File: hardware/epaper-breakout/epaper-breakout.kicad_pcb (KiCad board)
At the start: 2 copper layers, 99.6 x 31.2 mm, 68 parts, among them J1 XF2M-3315-1A, J2 C10418, J3 Conn_02x06_Counter_Clockwise, J4 ED060SC4, Q1 IRLML6402, U1 MCP1700-3302E_SOT23, U2 LT1945, U3 LT1945, U5 ESP32-WROVER, U6 CH330N, U7 LM358, U8 74HC4094-normal, U9 MCP9700AT-ETT

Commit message: WIP: partial routing
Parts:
- removed BOOT1: SW2, epaper-breakout:SW_TS-1187A
- removed RESET1: SW1, epaper-breakout:SW_TS-1187A
- added Q2: AO3401A, Package_TO_SOT_SMD:SOT-23, F.Cu at (70.9, 77.8)
- added Q3: MMBT3904, Package_TO_SOT_SMD:SOT-23, F.Cu at (38.4, 64.8)
- added Q4: MMBT3904, Package_TO_SOT_SMD:SOT-23, F.Cu at (34.0, 69.4)
- added Q5: AO3401A, Package_TO_SOT_SMD:SOT-23, F.Cu at (75.4, 77.8)
- added Q6: MMBT3904, Package_TO_SOT_SMD:SOT-23, F.Cu at (68.3, 70.3)
- added R1: 10k, Resistor_SMD:R_0805_2012Metric, F.Cu at (38.4, 68.6)
- added R20: 10k, Resistor_SMD:R_0805_2012Metric, F.Cu at (70.9, 81.5)
- added R21: 10k, Resistor_SMD:R_0805_2012Metric, F.Cu at (75.3, 81.5)
- added U10: ED060SC7, epaper-breakout:AXT334124, F.Cu at (118.6, 57.5)
- added U4: CH340G, Package_SO:SOIC-16_3.9x9.9mm_P1.27mm, F.Cu at (27.5, 68.3)
- added Y1: Crystal_GND2, Crystal:Crystal_SMD_3225-4Pin_3.2x2.5mm_HandSoldering, F.Cu at (60.9, 70.2)
- C13, C14: value 0.1uF -> 10pF
- C15, C16: value 1nF -> 0.1uF
- J4: moved to F.Cu
- Q1: value IRLML6402 -> MMBT3904
- R11: value 470 -> 10k
- R12: value 470 -> 1k
- U6: value CH330N -> ED060XC5; footprint Package_SO:SOIC-8_3.9x4.9mm_P1.27mm -> epaper-breakout:X05A20H34G
- moved R11 61.0 mm to (42.8, 68.6), turned to 0 degrees
- moved U6 49.3 mm to (70.6, 54.7), turned to 0 degrees
- moved Q1 44.3 mm to (66.5, 77.8), turned to 0 degrees
- moved U9 36.1 mm to (83.7, 21.7)
- moved R12 33.2 mm to (66.5, 81.5), turned to 0 degrees
- moved U8 30.9 mm to (77.2, 25.1)
- moved C16 27.1 mm to (42.6, 71.3), turned to 0 degrees
- moved J4 23.9 mm to (104.3, 56.1), turned to 0 degrees
- moved U5 22.8 mm to (95.9, 26.2), turned to 0 degrees
- moved C15 18.6 mm to (82.3, 67.9)
- moved R10 16.9 mm to (79.1, 66.3)
- moved R13 16.5 mm to (94.7, 8.20)
- moved R15 15.1 mm to (90.1, 9.80)
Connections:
- C1 pad 1: EPD_POWER -> SW_VIN
- C13 pad 1: /+3.3V -> Net-(C13-Pad1)
- C14 pad 1: /+3.3V -> GND
- C14 pad 2: GND -> Net-(C14-Pad2)
- C15 pad 1: GND -> /EN
- C15 pad 2: /EN -> GND
- C16 pad 1: GND -> /+3.3V
- C16 pad 2: Net-(C16-Pad2) -> GND
- C6 pad 1: EPD_POWER -> SW_VIN
- J1 pad 11: /+3.3V -> EPD_VDD
- J1 pad 30: /+3.3V -> EPD_VDD
- J1 pad 7: /+3.3V -> EPD_VDD
- J4 pad 10: /+3.3V -> EPD_VDD
- J4 pad 29: /+3.3V -> EPD_VDD
- J4 pad 30: /+3.3V -> EPD_VDD
- J4 pad 35: /+3.3V -> EPD_VDD
- J4 pad 36: /+3.3V -> EPD_VDD
- J4 pad 4: /+3.3V -> EPD_VDD
- J4 pad 8: /+3.3V -> EPD_VDD
- L1 pad 2: EPD_POWER -> SW_VIN
- L2 pad 2: EPD_POWER -> SW_VIN
- L3 pad 2: EPD_POWER -> SW_VIN
- L4 pad 2: EPD_POWER -> SW_VIN
- Q1 pad 1: /~SMPS_CTRL -> Net-(Q1-Pad1)
- Q1 pad 2: 5V -> GND
- Q1 pad 3: EPD_POWER -> Net-(Q1-Pad3)
- R11 pad 1: /EP_D3 -> Net-(Q4-Pad1)
- R11 pad 2: Net-(BOOT1-Pad2) -> /~RTS
- R12 pad 1: /EN -> Net-(Q1-Pad1)
- R12 pad 2: Net-(C16-Pad2) -> /SMPS_CTRL
- U2 pad 8: EPD_POWER -> SW_VIN
- U3 pad 8: EPD_POWER -> SW_VIN
- U6 pad 1: Net-(J2-Pad3) -> /-15V
- U6 pad 2: Net-(J2-Pad2) -> /-20V
- U6 pad 5: /+3.3V -> (no net)
- U6 pad 6: /USB_TXD -> EPD_VDD
- U6 pad 7: /USB_RXD -> GND
- U6 pad 8: /+3.3V -> /EP_CKH
- U8 pad 4: /~SMPS_CTRL -> /SMPS_CTRL
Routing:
- net /+3.3V: track 306.9 -> 8.42 mm, vias 13 -> 1
- net GND: track 368.8 -> 187.1 mm, vias 122 -> 62
- net /EP_STV: track 37.3 -> 139.0 mm, vias 1 -> 5
- net /+22V: track 115.5 -> 210.9 mm, vias 2 -> 7
- net EPD_VDD: track 0.00 -> 94.2 mm, vias 0 -> 6
- net /EP_MODE: track 46.7 -> 138.2 mm, vias 1 -> 5
- net SW_VIN: track 0.00 -> 81.7 mm, vias 0 -> 4
- net EPD_POWER: track 81.7 -> 0.00 mm, vias 4 -> 0
- net /A1: track 126.2 -> 46.3 mm, vias 1 -> 0
- net /EP_D6: track 41.9 -> 118.7 mm, vias 3 -> 6
- net /EP_D5: track 43.6 -> 117.2 mm, vias 3 -> 6
- net /EP_D7: track 48.5 -> 119.5 mm, vias 3 -> 5
- net /EP_D2: track 39.2 -> 109.3 mm, vias 1 -> 6
- net /EP_VCOM: track 95.0 -> 159.7 mm, vias 2 -> 6
- net /EP_OE: track 50.9 -> 114.4 mm, vias 3 -> 7
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- removed copper zone on B.Cu, net GND
- removed copper zone on F.Cu, net GND
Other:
- board size 99.6 x 31.2 mm -> 100 x 40.5 mm
- net class Default: clearance 0.2 -> 0.16
- rule trace_clearance: 0.2 -> 0.16

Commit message: partial routing
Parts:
- removed Q1: MMBT3904, Package_TO_SOT_SMD:SOT-23
- removed R2, R21, R3, R8, R9: 10k, Resistor_SMD:R_0805_2012Metric
- moved R12 53.3 mm to (70.6, 28.4), turned to 90 degrees
- moved R20 51.7 mm to (44.8, 36.8), turned to 180 degrees
- moved Q2 51.6 mm to (43.9, 33.8), turned to 270 degrees
- moved R13 49.7 mm to (108.0, 56.1), turned to 270 degrees
- moved R15 46.2 mm to (108.0, 52.4), turned to 90 degrees
- moved C16 42.8 mm to (32.3, 29.7)
- moved Q6 38.1 mm to (69.8, 32.3), turned to 270 degrees
- moved Y1 36.9 mm to (34.5, 44.3), turned to 180 degrees
- moved Q5 35.3 mm to (78.7, 42.7)
- moved R11 33.8 mm to (35.8, 35.5), turned to 180 degrees
- moved Q4 33.5 mm to (39.3, 36.3)
- moved U4 32.2 mm to (29.4, 36.1)
- moved C15 30.6 mm to (78.7, 37.6), turned to 0 degrees
- moved R1 29.3 mm to (35.8, 39.3), turned to 180 degrees
- moved R10 26.7 mm to (78.7, 39.6), turned to 180 degrees
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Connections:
- Q4 pad 3: /EP_D3 -> /EP_D0
- Q5 pad 1: Net-(Q1-Pad3) -> Net-(Q2-Pad1)
- R13 pad 1: /EP_D4 -> /EP_LE
- R15 pad 1: /EP_D3 -> /+3.3V
- R15 pad 2: /+3.3V -> /EP_D0
- U5 pad 10: /EP_CKV -> Net-(U5-Pad10)
- U5 pad 11: /EP_STH -> /EP_CKV
- U5 pad 12: /EP_D5 -> /EP_STH
- U5 pad 23: /EP_LE -> /EP_CKH
- U5 pad 24: /EP_D4 -> /EP_LE
- U5 pad 25: /EP_D3 -> /EP_D0
- U5 pad 26: /EP_D2 -> /EP_D1
- U5 pad 29: /EP_CKH -> /EP_D2
- U5 pad 30: Net-(U5-Pad30) -> /EP_D3
- U5 pad 31: Net-(U5-Pad31) -> /EP_D4
- U5 pad 33: /EP_D6 -> /EP_D5
- U5 pad 36: /EP_D7 -> /EP_D6
- U5 pad 37: Net-(U5-Pad37) -> /EP_D7
- U5 pad 8: /EP_D1 -> Net-(U5-Pad8)
- U5 pad 9: /EP_D0 -> Net-(U5-Pad9)
- U8 pad 1: Net-(U5-Pad31) -> Net-(U5-Pad10)
- U8 pad 2: Net-(U5-Pad37) -> Net-(U5-Pad9)
- U8 pad 3: Net-(U5-Pad30) -> Net-(U5-Pad8)
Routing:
- net GND: track 187.1 -> 12.6 mm, vias 62 -> 2
- net EPD_VDD: track 94.2 -> 188.3 mm, vias 6 -> 11
- net 5V: track 81.2 -> 0.00 mm, vias 2 -> 0
- net /15V: track 198.9 -> 127.1 mm
- net /MISO: track 57.6 -> 0.00 mm
- net /EP_D4: track 54.1 -> 110.9 mm, vias 5 -> 6
- net Net-(Q2-Pad1): track 0.00 -> 56.3 mm, vias 0 -> 2
- net /+22V: track 210.9 -> 157.3 mm, vias 7 -> 6
- net /MOSI: track 52.5 -> 0.00 mm, vias 1 -> 0
- net /SCLK: track 52.1 -> 0.00 mm
- net /SENSOR_VN: track 52.1 -> 0.00 mm
- net /SENSOR_VP: track 47.8 -> 0.00 mm
- net /A0: track 47.0 -> 0.00 mm
- net /A1: track 46.3 -> 0.00 mm
- net /EP_D3: track 60.3 -> 106.0 mm, vias 6 -> 4
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
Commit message: more routing
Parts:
- added C21: 10uF, Capacitor_SMD:C_0603_1608Metric, F.Cu at (48.3, 45.6)
- added C22: 0.1uF, Capacitor_SMD:C_0603_1608Metric, F.Cu at (48.3, 47.4)
- added C23: 0.1uF, Capacitor_SMD:C_0603_1608Metric, F.Cu at (45.5, 57.8)
- added D7: 1N5817, Diode_SMD:D_SOD-123, F.Cu at (43.1, 38.9)
- added D8: LED GREEN, LED_SMD:LED_0805_2012Metric, F.Cu at (43.6, 54.7)
- added D9: LED RED, LED_SMD:LED_0805_2012Metric, F.Cu at (43.6, 52.6)
- added J5: Conn_01x02_Male, Connector_PinHeader_2.54mm:PinHeader_1x02_P2.54mm_Vertical, F.Cu at (51.4, 57.7)
- added Q1: AO3401A, Package_TO_SOT_SMD:SOT-23, F.Cu at (48.1, 41.6)
- added R2: 100k, Resistor_SMD:R_0805_2012Metric, F.Cu at (51.1, 38.6)
- added R21: 100, Resistor_SMD:R_0805_2012Metric, F.Cu at (55.6, 57.7)
- added R22: 1k, Resistor_SMD:R_0805_2012Metric, F.Cu at (38.9, 52.5)
- added R3: 1k, Resistor_SMD:R_0805_2012Metric, F.Cu at (47.3, 54.7)
- added R8: 1k, Resistor_SMD:R_0805_2012Metric, F.Cu at (47.4, 52.6)
- added R9: 2k, Resistor_SMD:R_0805_2012Metric, F.Cu at (42.2, 43.2)
- added U11: TP4056, epaper-breakout:TP4056_SOP-8-PP, F.Cu at (42.3, 47.2)
- added U12: FS312F-G, Package_TO_SOT_SMD:SOT-23-6, F.Cu at (39.2, 56.6)
- added U13: FS8205A, Package_SO:TSSOP-8_4.4x3mm_P0.65mm, F.Cu at (34.0, 54.5)
- moved R15 34.6 mm to (73.8, 47.1), turned to 270 degrees
- moved R13 8.29 mm to (114.3, 50.8)
- moved R20 1.31 mm to (46.1, 36.8)
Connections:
- J2 pad 1: 5V -> VBUS
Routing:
- net /+3.3V: track 2.11 -> 144.2 mm, vias 0 -> 5
- net /USB_TXD: track 0.00 -> 100.7 mm, vias 0 -> 2
- net /USB_RXD: track 0.00 -> 95.4 mm, vias 0 -> 2
- net /SCLK: track 0.00 -> 87.8 mm, vias 0 -> 1
- net /MOSI: track 0.00 -> 87.3 mm, vias 0 -> 2
- net /MISO: track 0.00 -> 86.9 mm, vias 0 -> 1
- net /A1: track 0.00 -> 83.9 mm, vias 0 -> 4
- net /SENSOR_VN: track 0.00 -> 78.9 mm, vias 0 -> 1
- net /SENSOR_VP: track 0.00 -> 78.4 mm, vias 0 -> 1
- net /A0: track 0.00 -> 76.3 mm, vias 0 -> 1
- net 5V: track 0.00 -> 73.0 mm, vias 0 -> 5
- net /EP_D0: track 96.6 -> 165.0 mm, vias 6 -> 9
- net /EN: track 0.00 -> 56.9 mm, vias 0 -> 4
- net GND: track 12.6 -> 51.6 mm
- net VBUS: track 0.00 -> 36.3 mm, vias 0 -> 2
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
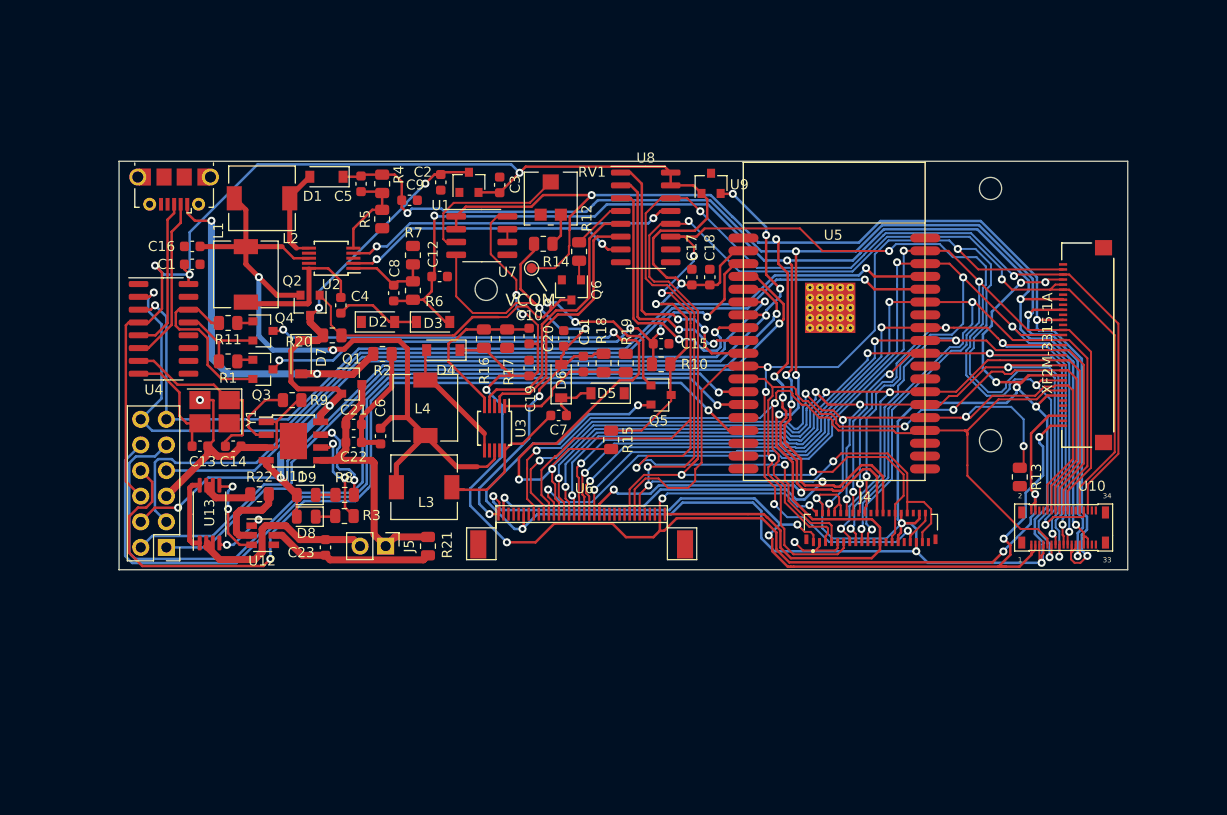
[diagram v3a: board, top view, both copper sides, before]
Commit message: remove battery protection, simplify
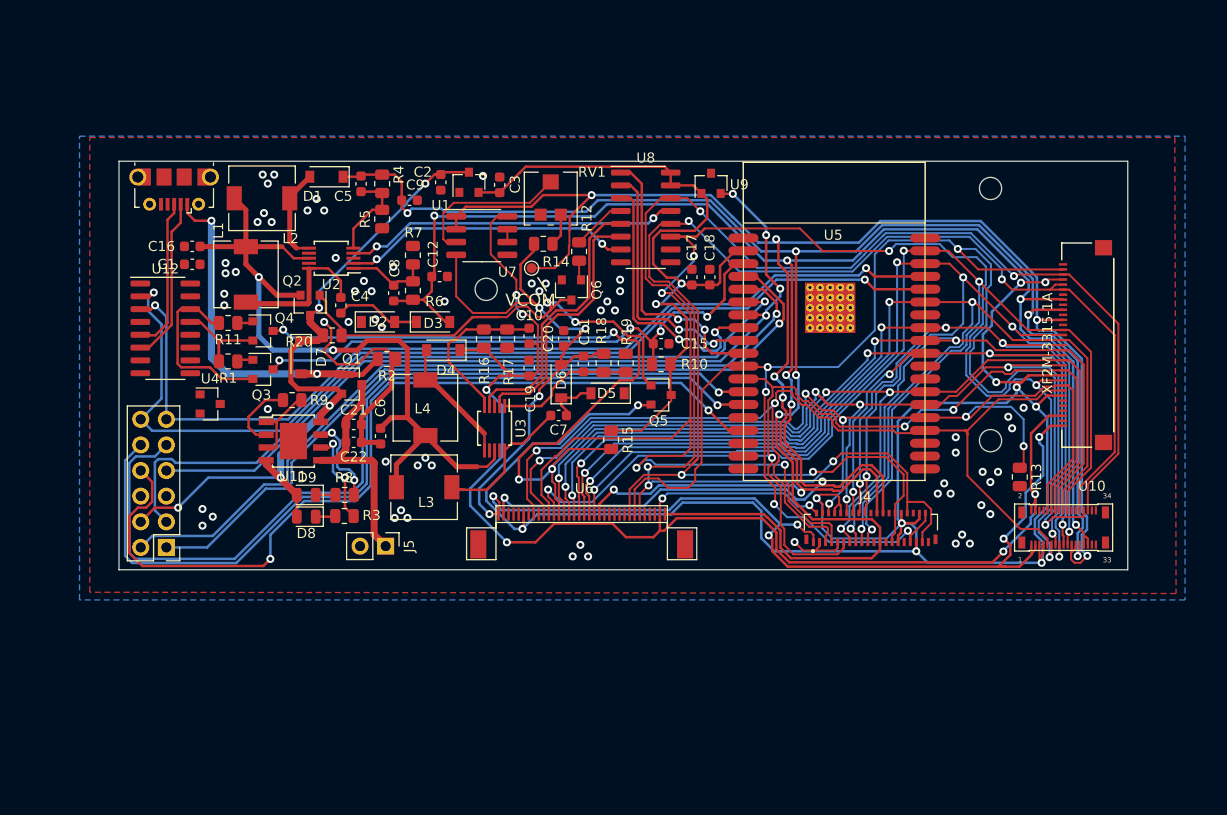
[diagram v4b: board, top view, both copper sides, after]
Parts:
- removed C13, C14: 10pF, Capacitor_SMD:C_0603_1608Metric
- removed C23: 0.1uF, Capacitor_SMD:C_0603_1608Metric
- removed R21: 100, Resistor_SMD:R_0805_2012Metric
- removed R22: 1k, Resistor_SMD:R_0805_2012Metric
- removed U13: FS8205A, Package_SO:TSSOP-8_4.4x3mm_P0.65mm
- removed Y1: Crystal_GND2, Crystal:Crystal_SMD_3225-4Pin_3.2x2.5mm_HandSoldering
- R9: value 2k -> 6.8k
- U12: value FS312F-G -> CH340C; footprint Package_TO_SOT_SMD:SOT-23-6 -> Package_SO:SOIC-16_3.9x9.9mm_P1.27mm
- U4: value CH340G -> XC6206PxxxMR; footprint Package_SO:SOIC-16_3.9x9.9mm_P1.27mm -> Package_TO_SOT_SMD:SOT-23
- moved U12 22.7 mm to (29.6, 36.1)
- moved U4 8.76 mm to (34.0, 43.6)
- moved R2 0.68 mm to (51.6, 39.1)
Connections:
- net 5V renamed VIN
- C1 pad 2: GND -> BAT-
- C12 pad 1: GND -> BAT-
- C15 pad 2: GND -> BAT-
- C16 pad 1: /+3.3V -> /+3.3_Serial
- C16 pad 2: GND -> BAT-
- C17 pad 2: GND -> BAT-
- C18 pad 1: GND -> BAT-
- C19 pad 1: GND -> BAT-
- C2 pad 1: GND -> BAT-
- C20 pad 1: GND -> BAT-
- C21 pad 2: GND -> BAT-
- C22 pad 1: GND -> BAT-
- C3 pad 1: GND -> BAT-
- C6 pad 2: GND -> BAT-
- C9 pad 1: GND -> BAT-
- D2 pad 1: GND -> BAT-
- D5 pad 1: GND -> BAT-
- J1 pad 33: GND -> BAT-
- J1 pad 5: GND -> BAT-
- J2 pad 5: GND -> BAT-
- J2 pad 6: GND -> BAT-
- J3 pad 5: GND -> BAT-
- J4 pad 3: GND -> BAT-
- J4 pad 31: GND -> BAT-
- J4 pad 34: GND -> BAT-
- J4 pad 9: GND -> BAT-
- Q6 pad 2: GND -> BAT-
- R13 pad 2: GND -> BAT-
- R17 pad 2: GND -> BAT-
- R19 pad 2: GND -> BAT-
- R2 pad 1: GND -> BAT-
- R5 pad 2: GND -> BAT-
- R7 pad 2: GND -> BAT-
- R9 pad 1: GND -> BAT-
- RV1 pad 1: GND -> BAT-
- U1 pad 1: GND -> BAT-
- U10 pad 31: GND -> BAT-
- U10 pad 32: GND -> BAT-
- U10 pad 6: GND -> BAT-
- U10 pad 8: GND -> BAT-
- U11 pad 1: GND -> BAT-
- U11 pad 3: GND -> BAT-
- U12 pad 1: Net-(U12-Pad1) -> BAT-
- U12 pad 2: Net-(R22-Pad2) -> /USB_TXD
- U12 pad 3: Net-(U12-Pad3) -> /USB_RXD
- U12 pad 4: (no net) -> /+3.3_Serial
- U12 pad 5: Net-(C23-Pad2) -> Net-(J2-Pad3)
- U12 pad 6: BAT- -> Net-(J2-Pad2)
- U2 pad 3: GND -> BAT-
- U2 pad 7: GND -> BAT-
- U2 pad 9: GND -> BAT-
- U3 pad 3: GND -> BAT-
- U3 pad 7: GND -> BAT-
- U3 pad 9: GND -> BAT-
- U4 pad 1: GND -> BAT-
- U4 pad 2: /USB_TXD -> /+3.3_Serial
- U4 pad 3: /USB_RXD -> VBUS
- U5 pad 1: GND -> BAT-
- U5 pad 15: GND -> BAT-
- U5 pad 38: GND -> BAT-
- U5 pad 39: GND -> BAT-
- U6 pad 26: GND -> BAT-
- U6 pad 3: GND -> BAT-
- U6 pad 31: GND -> BAT-
- U6 pad 32: GND -> BAT-
- U6 pad 7: GND -> BAT-
- U6 pad 9: GND -> BAT-
- U7 pad 5: GND -> BAT-
- U8 pad 8: GND -> BAT-
- U9 pad 3: GND -> BAT-
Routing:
- net /+3.3V: track 144.2 -> 71.7 mm, vias 5 -> 2
- net GND: track 51.6 -> 0.00 mm, vias 2 -> 61
- net BAT-: track 20.3 -> 38.6 mm, vias 0 -> 3
- net Net-(C14-Pad2): track 17.8 -> 0.00 mm
- net Net-(C23-Pad2): track 16.5 -> 0.00 mm
- net Net-(C13-Pad1): track 12.1 -> 0.00 mm
- net Net-(U12-Pad3): track 8.98 -> 0.00 mm, vias 2 -> 0
- net Net-(R22-Pad2): track 8.00 -> 0.00 mm
- net Net-(U13-Pad1): track 7.41 -> 0.00 mm
- net Net-(U12-Pad1): track 5.94 -> 0.00 mm, vias 2 -> 0
- net BAT+: track 27.3 -> 22.8 mm
- net /~DTR: track 9.15 -> 11.0 mm
- net /~RTS: track 17.6 -> 18.2 mm
- added copper zone on B.Cu, net BAT-
- added copper zone on F.Cu, net BAT-

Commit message: add battery voltage sensing, routing
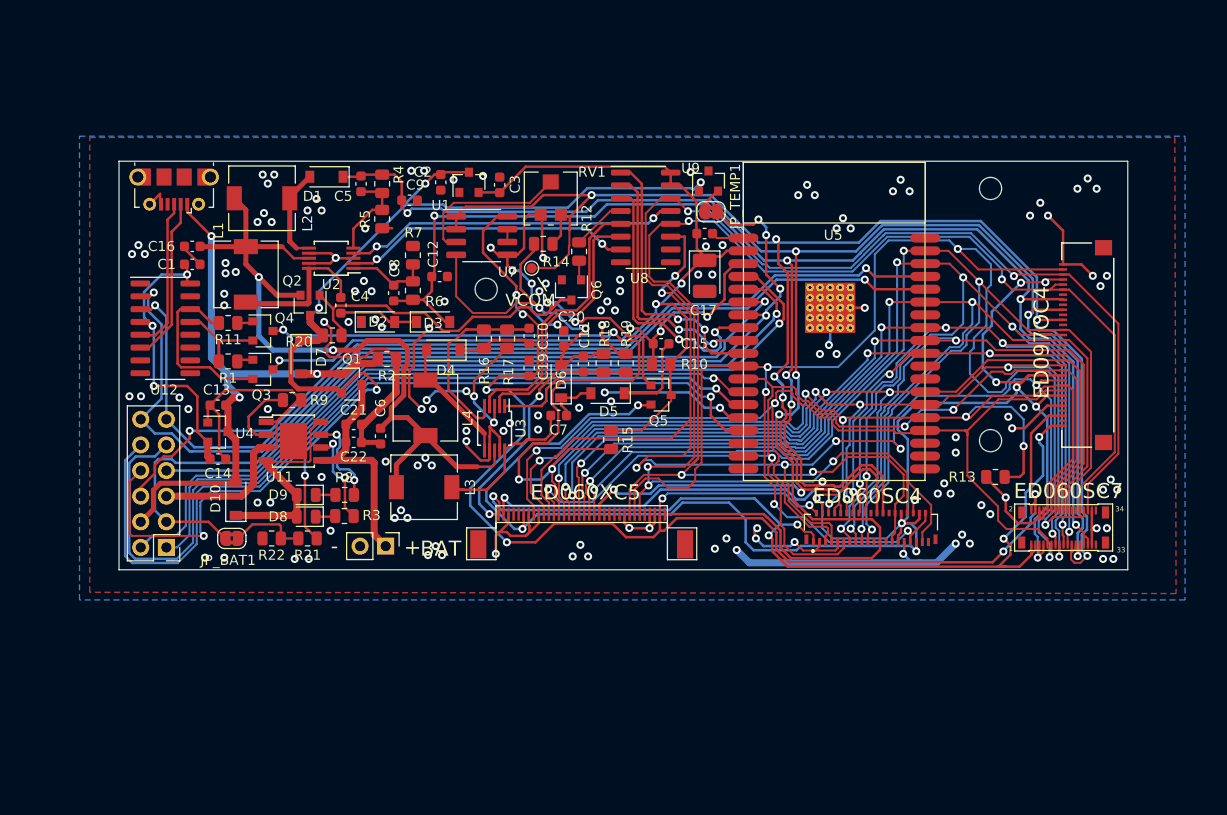
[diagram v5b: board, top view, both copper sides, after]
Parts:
- added C13: 1uF, Capacitor_SMD:C_0603_1608Metric, F.Cu at (34.8, 43.7)
- added C14: 1uF, Capacitor_SMD:C_0603_1608Metric, F.Cu at (34.8, 49.0)
- added D10: 1N5817, Diode_SMD:D_SOD-123, F.Cu at (36.6, 53.0)
- added JP_BAT1: Jumper, Jumper:SolderJumper-2_P1.3mm_Bridged2Bar_RoundedPad1.0x1.5mm, F.Cu at (36.2, 56.9)
- added JP_TEMP1: Jumper, Jumper:SolderJumper-2_P1.3mm_Bridged2Bar_RoundedPad1.0x1.5mm, F.Cu at (83.7, 24.5)
- added R21: 800k, Resistor_SMD:R_0805_2012Metric, F.Cu at (43.7, 56.9)
- added R22: 200k, Resistor_SMD:R_0805_2012Metric, F.Cu at (40.1, 56.9)
- C17: value 10uF -> 100uF; footprint Capacitor_SMD:C_0603_1608Metric -> Capacitor_Tantalum_SMD:CP_EIA-3528-15_AVX-H
- moved C18 4.35 mm to (83.1, 26.7), turned to 180 degrees
- moved U4 2.90 mm to (34.8, 46.4)
- moved R13 2.41 mm to (111.9, 50.8), turned to 180 degrees
- moved C17 1.28 mm to (83.1, 30.9), turned to 270 degrees
- moved U9 0.34 mm to (83.4, 21.5)
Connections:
- C1 pad 2: BAT- -> GND
- C12 pad 1: BAT- -> GND
- C15 pad 2: BAT- -> GND
- C16 pad 2: BAT- -> GND
- C17 pad 2: BAT- -> GND
- C18 pad 1: BAT- -> GND
- C19 pad 1: BAT- -> GND
- C2 pad 1: BAT- -> GND
- C20 pad 1: BAT- -> GND
- C21 pad 2: BAT- -> GND
- C22 pad 1: BAT- -> GND
- C3 pad 1: BAT- -> GND
- C6 pad 2: BAT- -> GND
- C9 pad 1: BAT- -> GND
- D2 pad 1: BAT- -> GND
- D5 pad 1: BAT- -> GND
- D8 pad 2: VIN -> Net-(D10-Pad1)
- D9 pad 2: VIN -> Net-(D10-Pad1)
- J1 pad 33: BAT- -> GND
- J1 pad 5: BAT- -> GND
- J2 pad 5: BAT- -> GND
- J2 pad 6: BAT- -> GND
- J3 pad 4: VIN -> VBUS
- J3 pad 5: BAT- -> GND
- J4 pad 3: BAT- -> GND
- J4 pad 31: BAT- -> GND
- J4 pad 34: BAT- -> GND
- J4 pad 9: BAT- -> GND
- J5 pad 2: BAT- -> GND
- Q6 pad 2: BAT- -> GND
- R13 pad 2: BAT- -> GND
- R17 pad 2: BAT- -> GND
- R19 pad 2: BAT- -> GND
- R2 pad 1: BAT- -> GND
- R5 pad 2: BAT- -> GND
- R7 pad 2: BAT- -> GND
- R9 pad 1: BAT- -> GND
- RV1 pad 1: BAT- -> GND
- U1 pad 1: BAT- -> GND
- U10 pad 31: BAT- -> GND
- U10 pad 32: BAT- -> GND
- U10 pad 6: BAT- -> GND
- U10 pad 8: BAT- -> GND
- U11 pad 1: BAT- -> GND
- U11 pad 3: BAT- -> GND
- U11 pad 4: VIN -> Net-(D10-Pad1)
- U11 pad 8: VIN -> Net-(D10-Pad1)
- U12 pad 1: BAT- -> GND
- U2 pad 3: BAT- -> GND
- U2 pad 7: BAT- -> GND
- U2 pad 9: BAT- -> GND
- U3 pad 3: BAT- -> GND
- U3 pad 7: BAT- -> GND
- U3 pad 9: BAT- -> GND
- U4 pad 1: BAT- -> GND
- U5 pad 1: BAT- -> GND
- U5 pad 15: BAT- -> GND
- U5 pad 38: BAT- -> GND
- U5 pad 39: BAT- -> GND
- U6 pad 26: BAT- -> GND
- U6 pad 3: BAT- -> GND
- U6 pad 31: BAT- -> GND
- U6 pad 32: BAT- -> GND
- U6 pad 7: BAT- -> GND
- U6 pad 9: BAT- -> GND
- U7 pad 5: BAT- -> GND
- U8 pad 8: BAT- -> GND
- U9 pad 1: /+3.3V -> VIN
- U9 pad 2: /A1 -> Net-(JP_TEMP1-Pad1)
- U9 pad 3: BAT- -> GND
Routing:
- net GND: track 0.00 -> 257.4 mm, vias 61 -> 147
- net /+3.3V: track 71.7 -> 122.6 mm, vias 2 -> 3
- net BAT-: track 38.6 -> 0.00 mm, vias 3 -> 0
- net /+3.3_Serial: track 0.00 -> 29.7 mm, vias 0 -> 3
- net VBUS: track 36.6 -> 60.4 mm, vias 2 -> 3
- net /EP_OE: track 156.3 -> 133.4 mm, vias 7 -> 8
- net Net-(D10-Pad1): track 0.00 -> 21.9 mm
- net VIN: track 73.0 -> 93.4 mm
- net EPD_VDD: track 188.3 -> 174.3 mm
- net /MOSI: track 87.3 -> 79.4 mm
- net Net-(JP_BAT1-Pad2): track 0.00 -> 7.83 mm
- net /A0: track 76.3 -> 82.8 mm
- net /15V: track 145.1 -> 149.4 mm
- net Net-(Q2-Pad1): track 46.8 -> 51.1 mm
- net /EP_D0: track 165.0 -> 168.2 mm
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- added copper zone on B.Cu, net GND
- added copper zone on F.Cu, net GND
- removed copper zone on B.Cu, net BAT-
- removed copper zone on F.Cu, net BAT-
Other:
- board text added: "+"
- board text added: "-"
- board text added: "BAT"
- board text added: "ED060SC4"
- board text added: "ED060SC7"
- board text added: "ED060XC5"
- board text added: "ED097OC4"
- board text added: "EPaper Breakout v5 by Valentin Roland 2021"
- board text removed: "EPaper Breakout v4 by Valentin Roland 2020"
